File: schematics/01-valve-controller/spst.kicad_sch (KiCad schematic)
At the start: 5 parts, among them K201 SPST Relay, Q201 BSS138

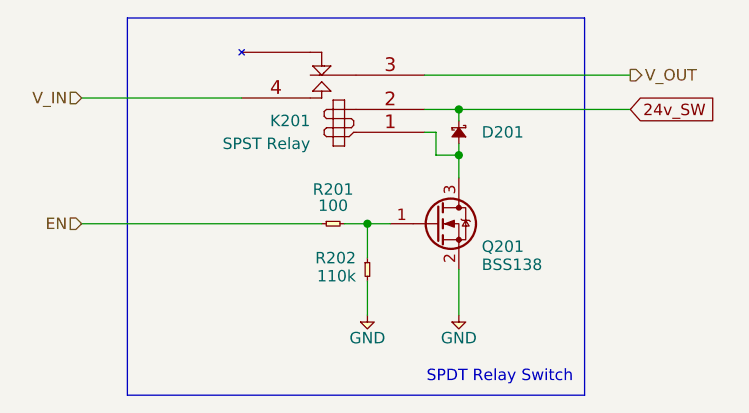
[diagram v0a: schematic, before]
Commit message: Flatten directory structure
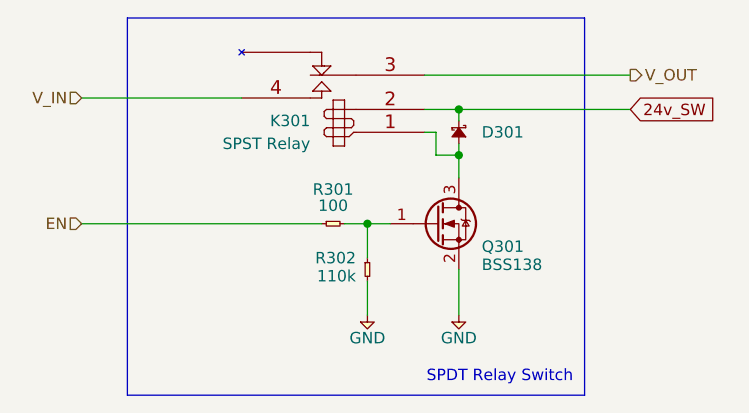
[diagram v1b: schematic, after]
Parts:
- renumbered D201 to D301, K201 to K301, Q201 to Q301, R201 to R301, R202 to R302
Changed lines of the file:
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@@
   (symbol (lib_id "royale:Diode_Schottky") (at 147.32 67.31 270)
     (in_bom yes) (on_board yes)
-    (property "Reference" "D201" (id 0) (at 149.86 68.58 90)
+    (property "Reference" "D301" (id 0) (at 149.86 68.58 90)
       (effects (font (size 1.27 1.27)) (justify left))
     )
@@
   (symbol (lib_id "royale:Relay_SPST") (at 133.35 68.58 0) (mirror y)
     (in_bom yes) (on_board yes)
-    (property "Reference" "K201" (id 0) (at 130.81 67.31 0)
+    (property "Reference" "K301" (id 0) (at 130.81 67.31 0)
       (effects (font (size 1.27 1.27)) (justify left))
     )
@@
   (symbol (lib_id "royale:BSS138") (at 144.78 78.74 0)
     (in_bom yes) (on_board yes)
-    (property "Reference" "Q201" (id 0) (at 149.86 81.28 0)
+    (property "Reference" "Q301" (id 0) (at 149.86 81.28 0)
       (effects (font (size 1.27 1.27)) (justify left))
     )
@@
   (symbol (lib_id "royale:GND") (at 147.32 88.9 0)
     (in_bom yes) (on_board yes)
-    (property "Reference" "#PWR0202" (id 0) (at 144.018 87.884 0)
+    (property "Reference" "#PWR0302" (id 0) (at 144.018 87.884 0)
       (effects (font (size 1.27 1.27)) (justify left) hide)
     )
@@
   (symbol (lib_id "royale:R") (at 132.08 78.74 0)
     (in_bom yes) (on_board yes)
-    (property "Reference" "R201" (id 0) (at 133.35 74.93 0))
+    (property "Reference" "R301" (id 0) (at 133.35 74.93 0))
     (property "Value" "100" (id 1) (at 133.35 77.47 0)
       (effects (font (size 1.27 1.27)) (justify bottom))
@@
   (symbol (lib_id "royale:GND") (at 137.16 88.9 0)
     (in_bom yes) (on_board yes)
-    (property "Reference" "#PWR0201" (id 0) (at 133.858 87.884 0)
+    (property "Reference" "#PWR0301" (id 0) (at 133.858 87.884 0)
       (effects (font (size 1.27 1.27)) (justify left) hide)
     )
@@
   (symbol (lib_id "royale:R") (at 137.16 82.55 90) (mirror x)
     (in_bom yes) (on_board yes)
-    (property "Reference" "R202" (id 0) (at 135.89 82.55 90)
+    (property "Reference" "R302" (id 0) (at 135.89 82.55 90)
       (effects (font (size 1.27 1.27)) (justify left))
     )
